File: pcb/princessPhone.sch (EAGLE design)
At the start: 78 parts, among them P1 TC2030-MCP-NL, Q1 2N7002K, U1 Value, U2 AG1170-S3-VERTICAL, U3 PI32MX170D-PT, U4 BLUETOOTH-RN-52, X1 USB_MICRO_B, X3 XRJK-S-01-6-4-0-9M2

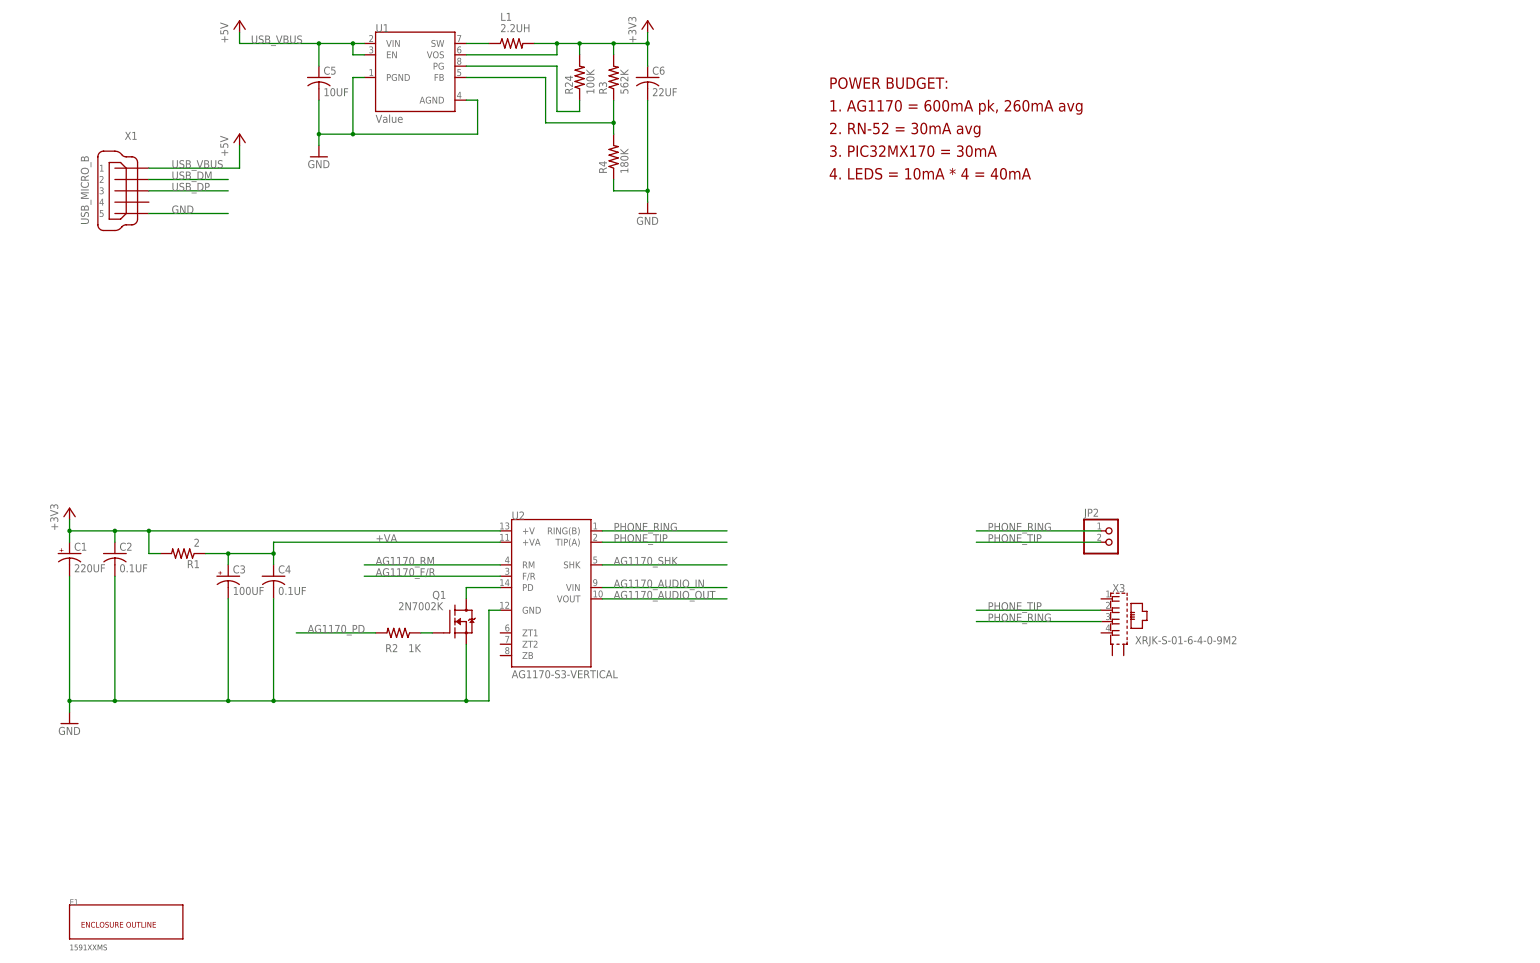
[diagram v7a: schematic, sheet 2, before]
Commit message: UPDATED USB/RJ-11/OUTLINE
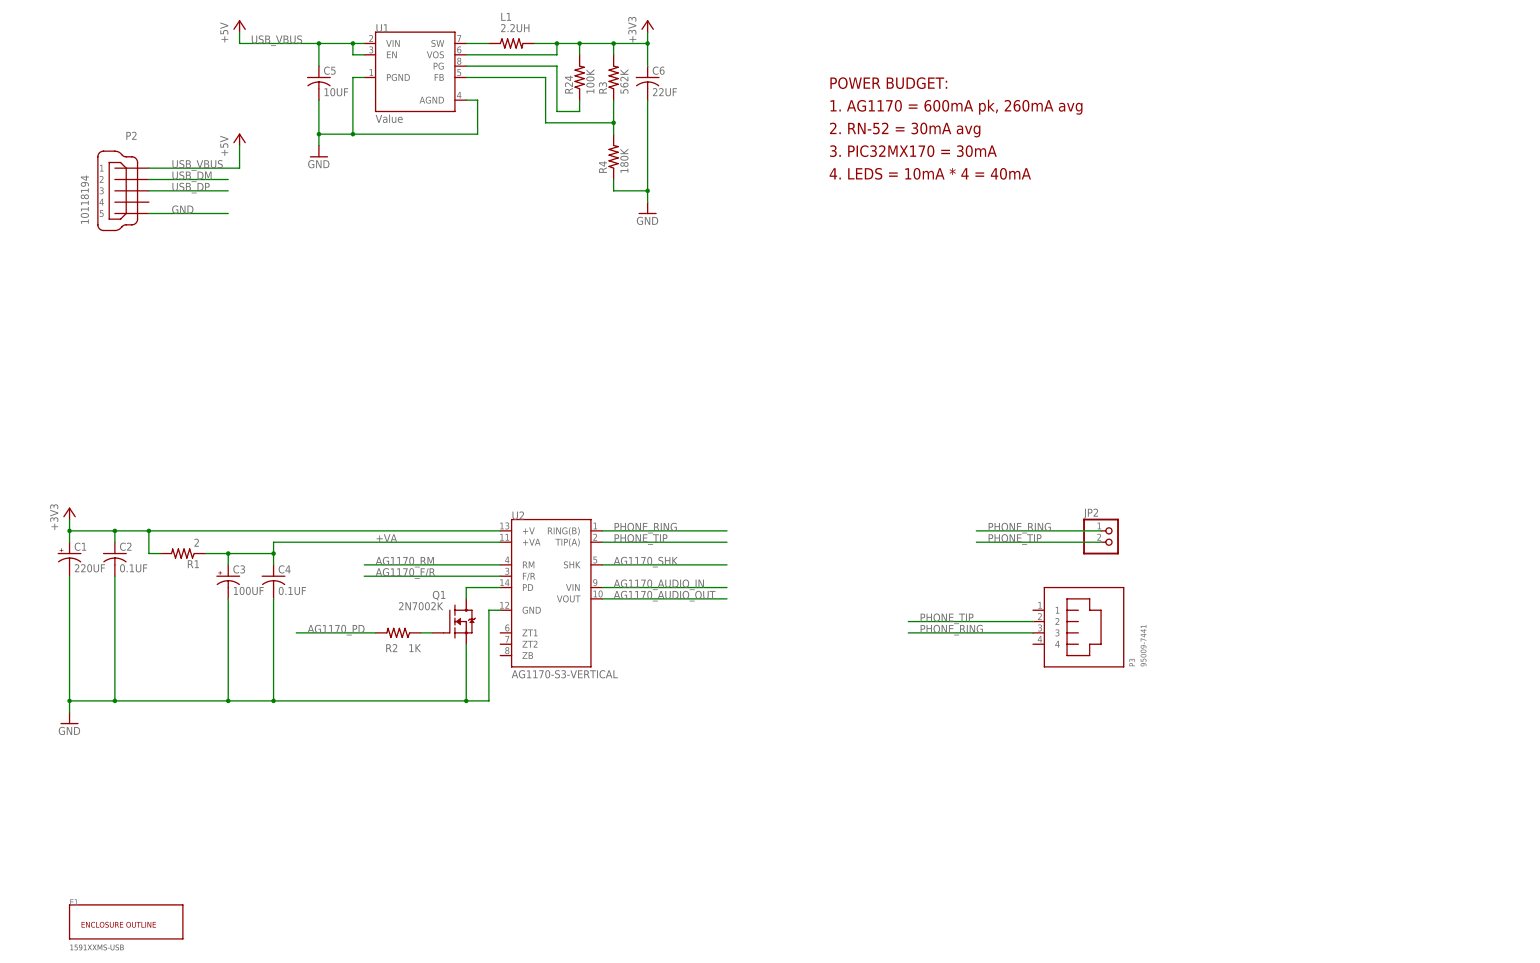
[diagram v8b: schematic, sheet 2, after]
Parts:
- removed X1: USB_MICRO_B, FosBattery1:USB_MICRO_B
- removed X3: XRJK-S-01-6-4-0-9M2, con-xmultiple:XRJK-S-01-6-4-0-9M2
- added P2: 10118194, console_board:10118194
- added P3: 95009-7441, princessPhone:95009-7441
- E1: value 1591XXMS -> 1591XXMS-USB; device princessPhone:1591XXMS -> princessPhone:1591XXMS-USB
- R14, R15: device rcl:R-US_R0603 -> rcl:R-US_R0402
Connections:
- net GND: now also P2.5; no longer X1.5
- net PHONE_RING: now also P3.3; no longer X3.3
- net PHONE_TIP: now also P3.2; no longer X3.2
- net USB_DM: now also P2.2; no longer X1.2
- net USB_DP: now also P2.3; no longer X1.3
- net USB_VBUS: now also P2.1; no longer X1.1
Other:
- note added: "FINISHED ROUTING, UPDATED USB/RJ-11/BOARD OUTLINE"
- note removed: "FINISHED ROUTING"
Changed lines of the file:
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@@
 <part name="R4" library="rcl" deviceset="R-US_" device="R0603" value="180K"/>
 <part name="+3V32" library="supply1" deviceset="+3V3" device=""/>
-<part name="X1" library="FosBattery1" deviceset="USB_MICRO_B" device=""/>
 <part name="LED1" library="led" deviceset="LED" device="CHIPLED_0603" value="BLUE"/>
 <part name="LED2" library="led" deviceset="LED" device="CHIPLED_0603" value="RED"/>
@@
 <part name="GND10" library="supply1" deviceset="GND" device=""/>
 <part name="GND11" library="supply1" deviceset="GND" device=""/>
-<part name="R14" library="rcl" deviceset="R-US_" device="R0603" value="0"/>
-<part name="R15" library="rcl" deviceset="R-US_" device="R0603" value="0"/>
+<part name="R14" library="rcl" deviceset="R-US_" device="R0402" value="0"/>
+<part name="R15" library="rcl" deviceset="R-US_" device="R0402" value="0"/>
 <part name="R16" library="rcl" deviceset="R-US_" device="R0603" value="0"/>
 <part name="R17" library="rcl" deviceset="R-US_" device="R0603" value="0"/>
-<part name="X3" library="con-xmultiple" deviceset="XRJK*4" device="-0-9M2" technology="-S-01-6-"/>
 <part name="U3" library="raveGear5" deviceset="PI32MX1*D-PT" device="" technology="70"/>
 <part name="GND9" library="supply1" deviceset="GND" device=""/>
@@
 <part name="P+2" library="supply1" deviceset="+5V" device=""/>
 <part name="TP3" library="testpad" deviceset="PTR1" device="B1,27"/>
-<part name="E1" library="princessPhone" deviceset="1591XXMS" device=""/>
+<part name="E1" library="princessPhone" deviceset="1591XXMS" device="-USB" value="1591XXMS-USB"/>
 <part name="LED5" library="led" deviceset="LED" device="CHIPLED_0603" value="RED"/>
 <part name="LED6" library="led" deviceset="LED" device="CHIPLED_0603" value="GREEN"/>
@@
 <part name="SW2" library="switch-omron" deviceset="31-XX" device=""/>
 <part name="SW3" library="switch-omron" deviceset="31-XX" device=""/>
+<part name="P2" library="console_board" deviceset="10118194" device=""/>
+<part name="P3" library="princessPhone" deviceset="95009-7441" device=""/>
 </parts>
 <sheets>
@@
 <text x="50.8" y="165.1" size="2.54" layer="94">ANDERS NELSON</text>
 <text x="144.78" y="165.1" size="2.54" layer="94">2015.08.09</text>
-<text x="193.04" y="167.64" size="2.54" layer="94">FINISHED ROUTING</text>
+<text x="193.04" y="165.1" size="2.54" layer="94">FINISHED ROUTING, UPDATED USB/RJ-11/BOARD OUTLINE</text>
 </plain>
 <instances>
@@
 <attribute name="VALUE" x="218.44" y="251.46" size="1.778" layer="96" rot="R90"/>
 </instance>
-<instance part="X1" gate="G$1" x="104.14" y="218.44" smashed="yes" rot="MR0">
-<attribute name="NAME" x="106.68" y="229.87" size="1.778" layer="95" font="vector" rot="MR0"/>
-<attribute name="VALUE" x="93.98" y="210.82" size="1.778" layer="96" font="vector" rot="MR90"/>
-</instance>
-<instance part="X3" gate="G$1" x="330.2" y="121.92"/>
 <instance part="Q1" gate="G$1" x="177.8" y="121.92" smashed="yes">
 <attribute name="VALUE" x="165.1" y="124.46" size="1.778" layer="96"/>
@@
 <instance part="P+2" gate="1" x="129.54" y="256.54"/>
 <instance part="E1" gate="G$1" x="104.14" y="55.88"/>
+<instance part="P2" gate="G$1" x="101.6" y="218.44" rot="MR0"/>
+<instance part="P3" gate="G$1" x="320.04" y="121.92" rot="R90"/>
 </instances>
 <busses>
@@
 <wire x1="109.22" y1="213.36" x2="127" y2="213.36" width="0.1524" layer="91"/>
 <label x="114.3" y="213.36" size="1.778" layer="95"/>
-<pinref part="X1" gate="G$1" pin="5"/>
+<pinref part="P2" gate="G$1" pin="5"/>
 </segment>
 </net>
@@
 <wire x1="109.22" y1="218.44" x2="127" y2="218.44" width="0.1524" layer="91"/>
 <label x="114.3" y="218.44" size="1.778" layer="95"/>
-<pinref part="X1" gate="G$1" pin="3"/>
+<pinref part="P2" gate="G$1" pin="3"/>
 </segment>
 </net>
@@
 <wire x1="127" y1="220.98" x2="109.22" y2="220.98" width="0.1524" layer="91"/>
 <label x="114.3" y="220.98" size="1.778" layer="95"/>
-<pinref part="X1" gate="G$1" pin="2"/>
+<pinref part="P2" gate="G$1" pin="2"/>
 </segment>
 </net>
@@
 </segment>
 <segment>
-<wire x1="294.64" y1="121.92" x2="322.58" y2="121.92" width="0.1524" layer="91"/>
-<label x="297.18" y="121.92" size="1.778" layer="95"/>
-<pinref part="X3" gate="G$1" pin="3"/>
+<wire x1="279.4" y1="119.38" x2="307.34" y2="119.38" width="0.1524" layer="91"/>
+<label x="281.94" y="119.38" size="1.778" layer="95"/>
+<pinref part="P3" gate="G$1" pin="3"/>
 </segment>
 </net>
@@
 </segment>
 <segment>
-<wire x1="322.58" y1="124.46" x2="294.64" y2="124.46" width="0.1524" layer="91"/>
-<label x="297.18" y="124.46" size="1.778" layer="95"/>
-<pinref part="X3" gate="G$1" pin="2"/>
+<wire x1="307.34" y1="121.92" x2="279.4" y2="121.92" width="0.1524" layer="91"/>
+<label x="281.94" y="121.92" size="1.778" layer="95"/>
+<pinref part="P3" gate="G$1" pin="2"/>
 </segment>
 </net>
@@
 <wire x1="109.22" y1="223.52" x2="129.54" y2="223.52" width="0.1524" layer="91"/>
 <label x="114.3" y="223.52" size="1.778" layer="95"/>
-<pinref part="X1" gate="G$1" pin="1"/>
 <pinref part="P+1" gate="1" pin="+5V"/>
 <wire x1="129.54" y1="223.52" x2="129.54" y2="228.6" width="0.1524" layer="91"/>
-</segment>
-<segment>
+<pinref part="P2" gate="G$1" pin="1"/>
+</segment>
+<segment>
